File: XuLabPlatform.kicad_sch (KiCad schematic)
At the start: 15 parts, among them J10 Servo, J11 Servo, J12 Thruster, J14 I2C, J15 I2C, J16 UART1, J17 UART2, J18 SPI1, J19 SPI2, J4 Servo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

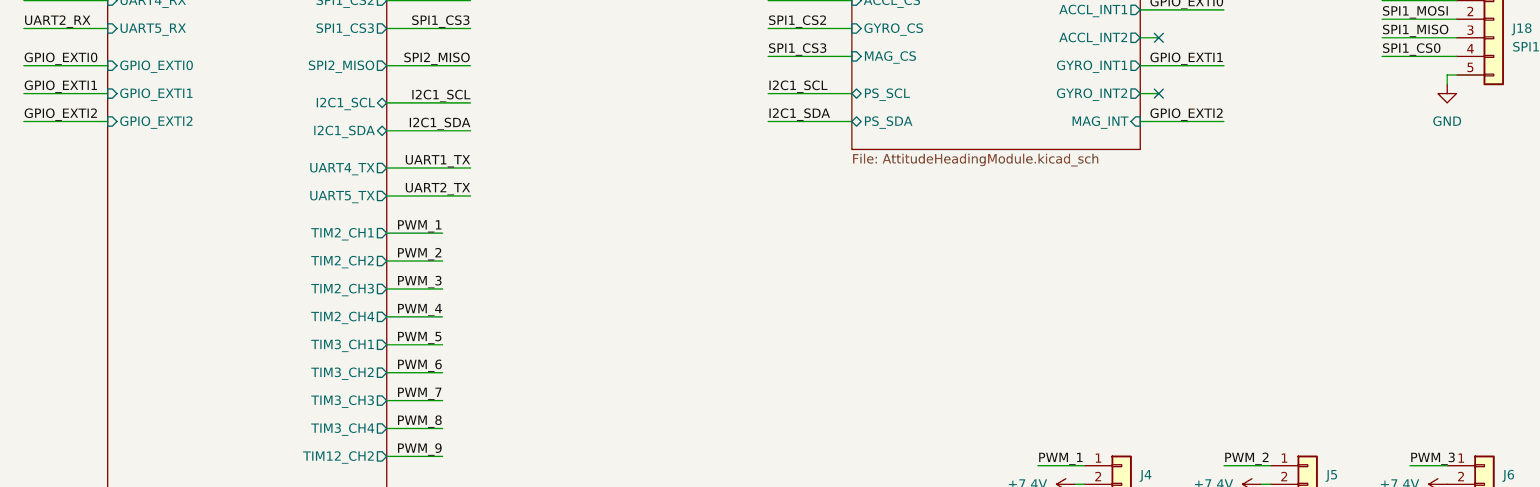
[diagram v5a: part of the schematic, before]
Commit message: Add extra interrupts and connector
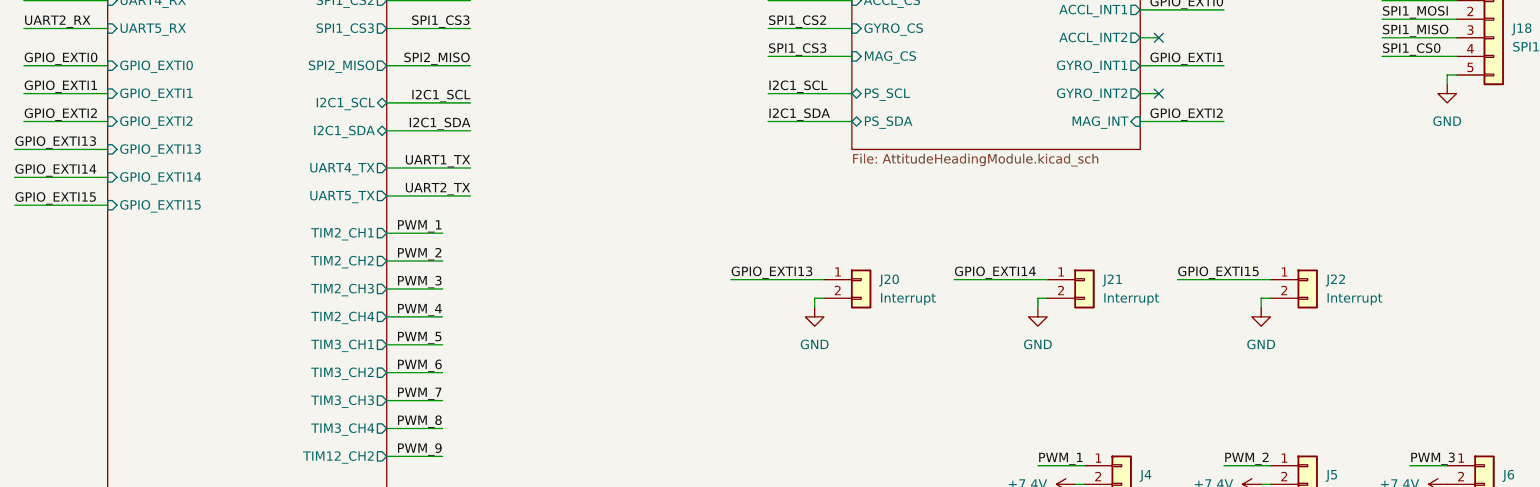
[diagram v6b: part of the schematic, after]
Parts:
- added J20, J21, J22: Interrupt, Connector_Molex:Molex_KK-254_AE-6410-02A_1x02_P2.54mm_Vertical, symbol Connector_Generic:Conn_01x02
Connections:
- net GND: now also J20.2 (Pin_2), J21.2 (Pin_2), J22.2 (Pin_2)
- new net GPIO_EXTI13: J20.1 (Pin_1)
- new net GPIO_EXTI14: J21.1 (Pin_1)
- new net GPIO_EXTI15: J22.1 (Pin_1)
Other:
- sheet MCU A ports: added GPIO_EXTI13, GPIO_EXTI14, GPIO_EXTI15; removed none

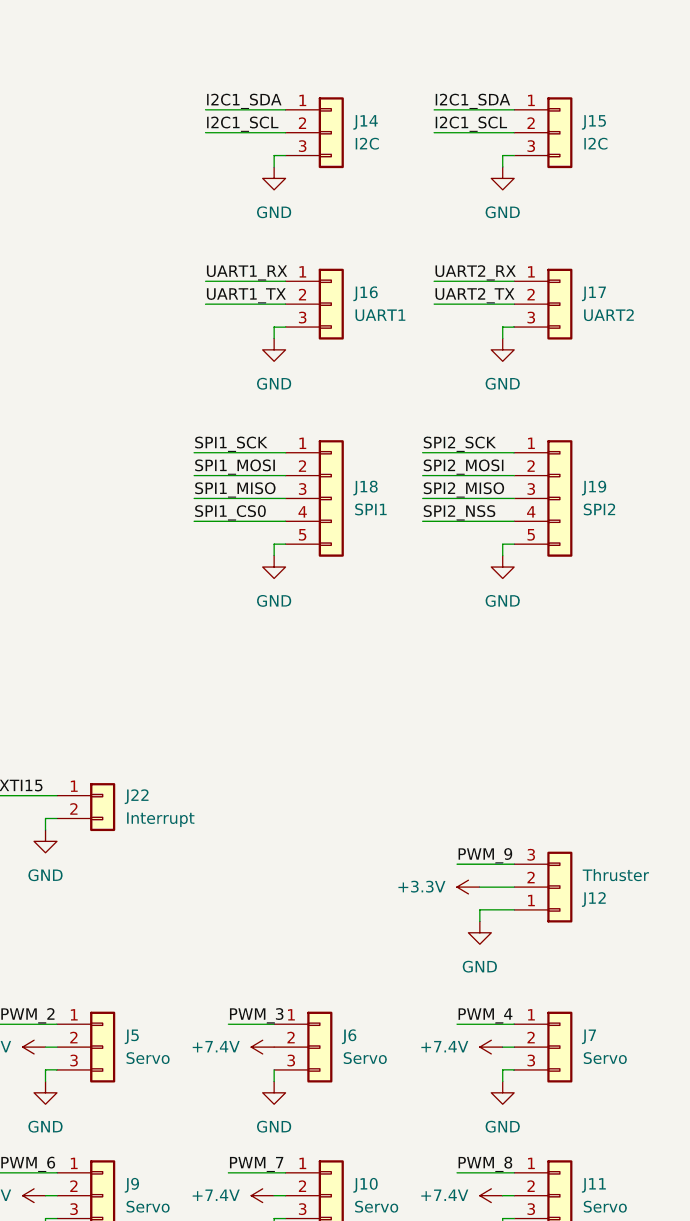
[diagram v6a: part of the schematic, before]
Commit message: Add 3.3 V pin to peripheral connectors
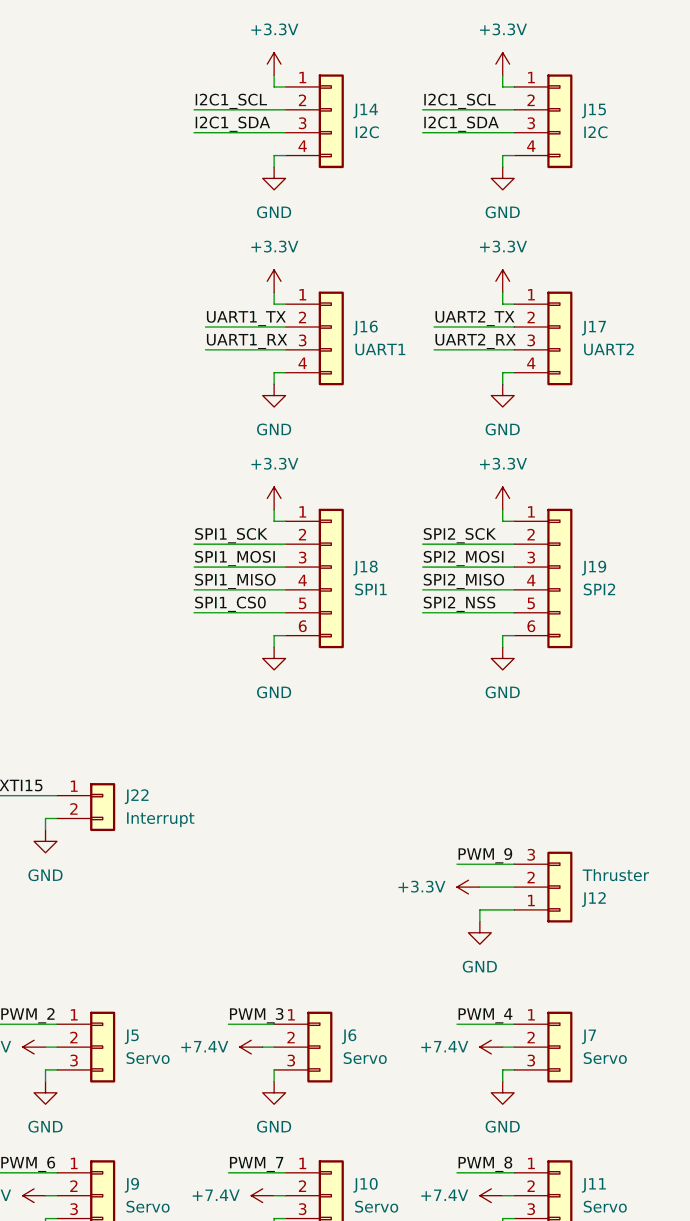
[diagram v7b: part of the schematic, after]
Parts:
- removed J14, J15: I2C, Connector_Molex:Molex_PicoBlade_53048-0310_1x03_P1.25mm_Horizontal, symbol Connector_Generic:Conn_01x03
- removed J16: UART1, Connector_Molex:Molex_PicoBlade_53048-0310_1x03_P1.25mm_Horizontal, symbol Connector_Generic:Conn_01x03
- removed J17: UART2, Connector_Molex:Molex_PicoBlade_53048-0310_1x03_P1.25mm_Horizontal, symbol Connector_Generic:Conn_01x03
- removed J18: SPI1, Connector_Molex:Molex_PicoBlade_53048-0510_1x05_P1.25mm_Horizontal, symbol Connector_Generic:Conn_01x05
- removed J19: SPI2, Connector_Molex:Molex_PicoBlade_53048-0510_1x05_P1.25mm_Horizontal, symbol Connector_Generic:Conn_01x05
- added J14, J15: I2C, Connector_Molex:Molex_PicoBlade_53048-0410_1x04_P1.25mm_Horizontal, symbol Connector_Generic:Conn_01x04
- added J16: UART1, Connector_Molex:Molex_PicoBlade_53048-0410_1x04_P1.25mm_Horizontal, symbol Connector_Generic:Conn_01x04
- added J17: UART2, Connector_Molex:Molex_PicoBlade_53048-0410_1x04_P1.25mm_Horizontal, symbol Connector_Generic:Conn_01x04
- added J18: SPI1, Connector_Molex:Molex_PicoBlade_53048-0610_1x06_P1.25mm_Horizontal, symbol Connector_Generic:Conn_01x06
- added J19: SPI2, Connector_Molex:Molex_PicoBlade_53048-0610_1x06_P1.25mm_Horizontal, symbol Connector_Generic:Conn_01x06
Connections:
- net +3.3V: now also J14.1 (Pin_1), J15.1 (Pin_1), J16.1 (Pin_1), J17.1 (Pin_1), J18.1 (Pin_1), J19.1 (Pin_1)
- net GND: now also J14.4 (Pin_4), J15.4 (Pin_4), J16.4 (Pin_4), J17.4 (Pin_4), J18.6 (Pin_6), J19.6 (Pin_6)
- net I2C1_SCL: now also J14.2 (Pin_2), J15.2 (Pin_2)
- net I2C1_SDA: now also J14.3 (Pin_3), J15.3 (Pin_3)
- net SPI1_CS0: now also J18.5 (Pin_5)
- net SPI1_MISO: now also J18.4 (Pin_4)
- net SPI1_MOSI: now also J18.3 (Pin_3)
- net SPI1_SCK: now also J18.2 (Pin_2)
- net SPI2_MISO: now also J19.4 (Pin_4)
- net SPI2_MOSI: now also J19.3 (Pin_3)
- net SPI2_NSS: now also J19.5 (Pin_5)
- net SPI2_SCK: now also J19.2 (Pin_2)
- net UART1_RX: now also J16.3 (Pin_3)
- net UART1_TX: now also J16.2 (Pin_2)
- net UART2_RX: now also J17.3 (Pin_3)
- net UART2_TX: now also J17.2 (Pin_2)

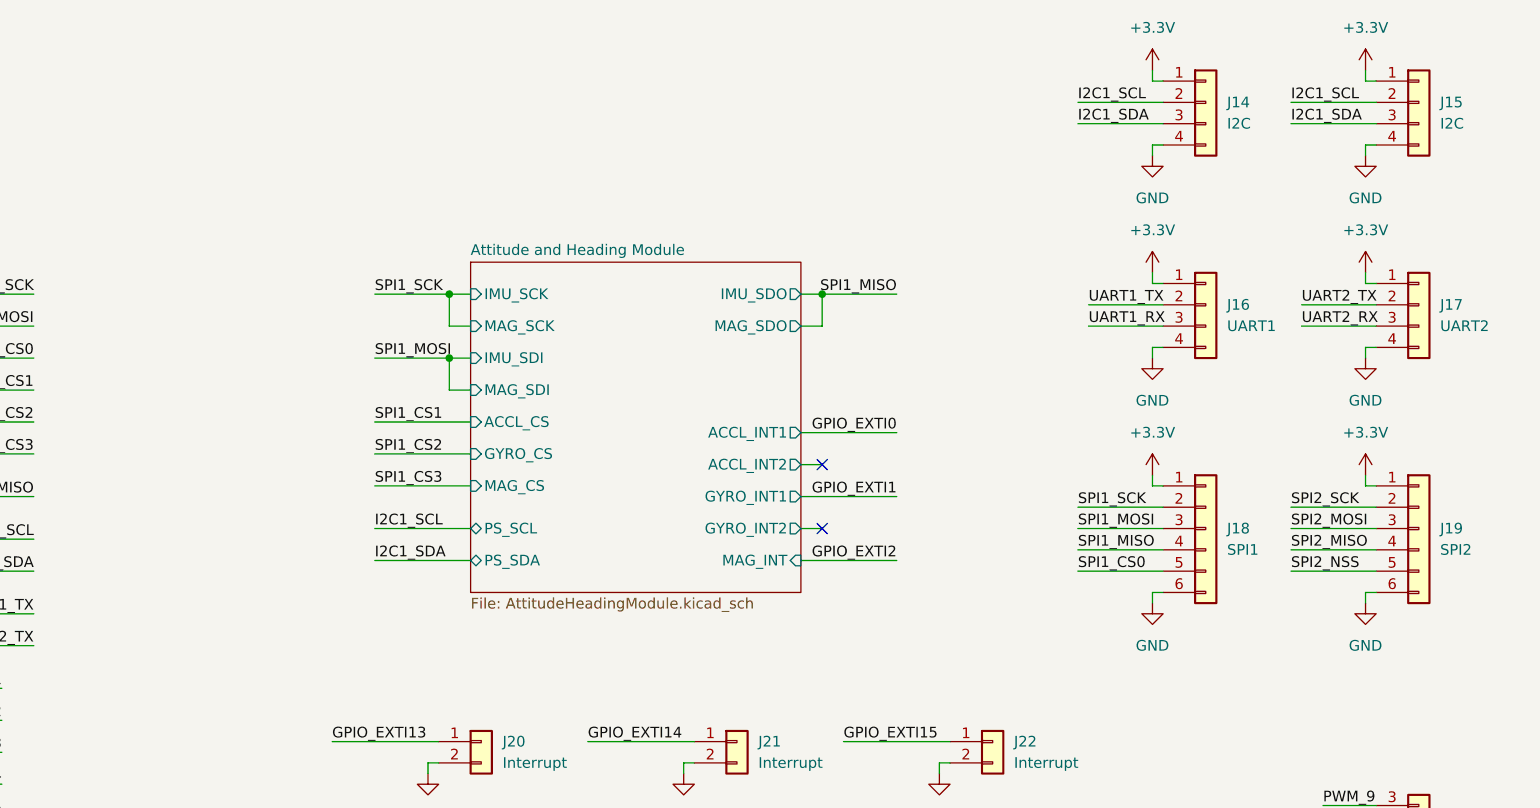
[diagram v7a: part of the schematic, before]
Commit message: Add 100nF capacitors to connectors
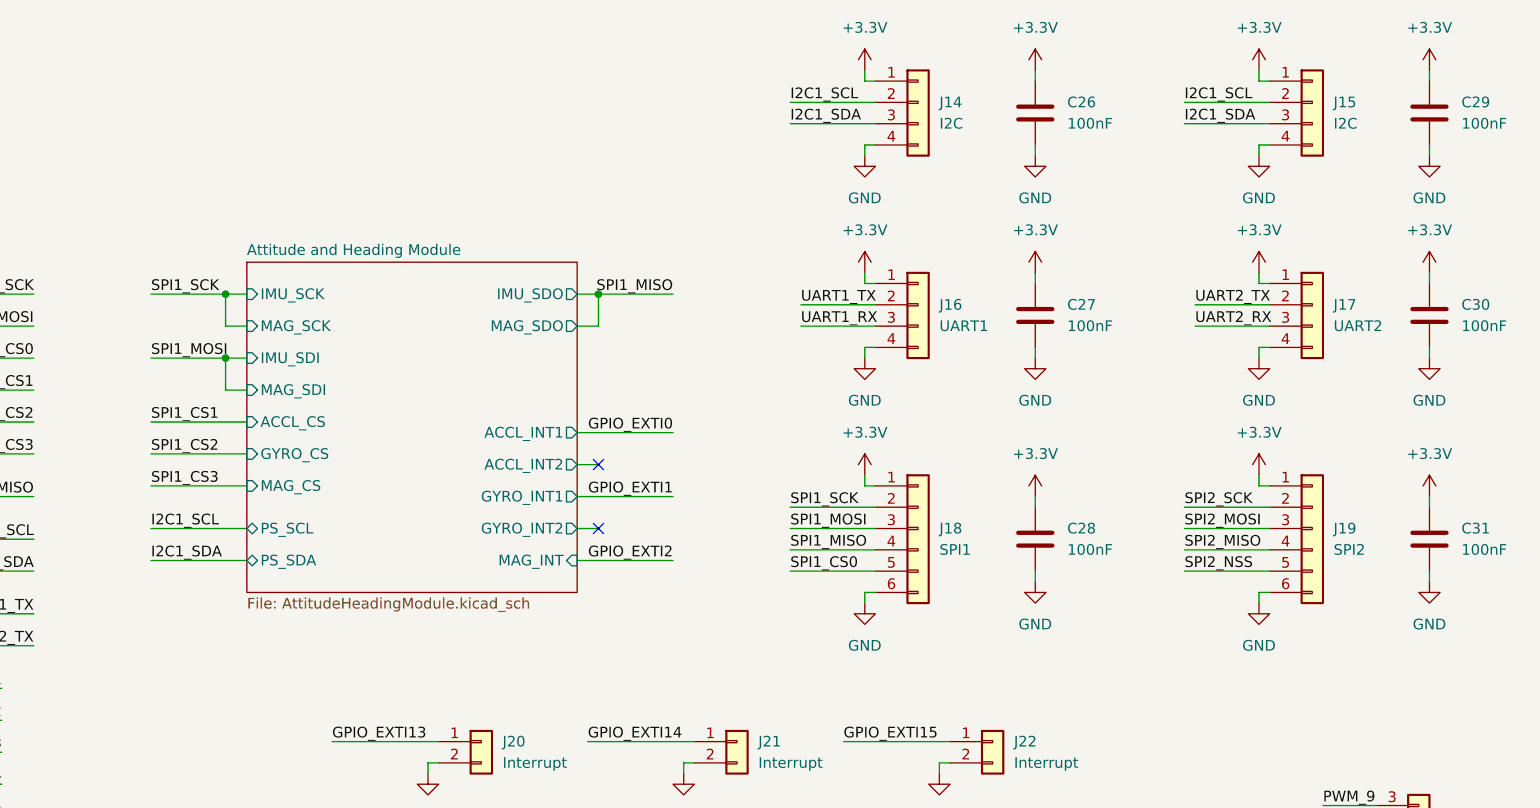
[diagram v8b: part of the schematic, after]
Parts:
- added C26, C27, C28, C29, C30, C31: 100nF, Capacitor_SMD:C_0402_1005Metric, symbol Device:C
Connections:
- net +3.3V: now also C26.1, C27.1, C28.1, C29.1, C30.1, C31.1
- net GND: now also C26.2, C27.2, C28.2, C29.2, C30.2, C31.2
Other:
- moved on the sheet: J14, J15, J16, J17, J18, J19
